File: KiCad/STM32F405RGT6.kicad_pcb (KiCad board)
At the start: 4 copper layers, 101.6 x 101.6 mm, 65 parts, among them J1 Conn_02x05_Odd_Even, J2 USB_C_2.0, J3 Conn_02x32_Odd_Even, J4 Conn_02x20_Odd_Even, Q1 AO3401A, SW1 TS-1187A, SW2 TS-1187A, U1 M24C02-RMN, U2 AMS1117-3.3, U3 STM32F405RGTx, Y1 16MHz

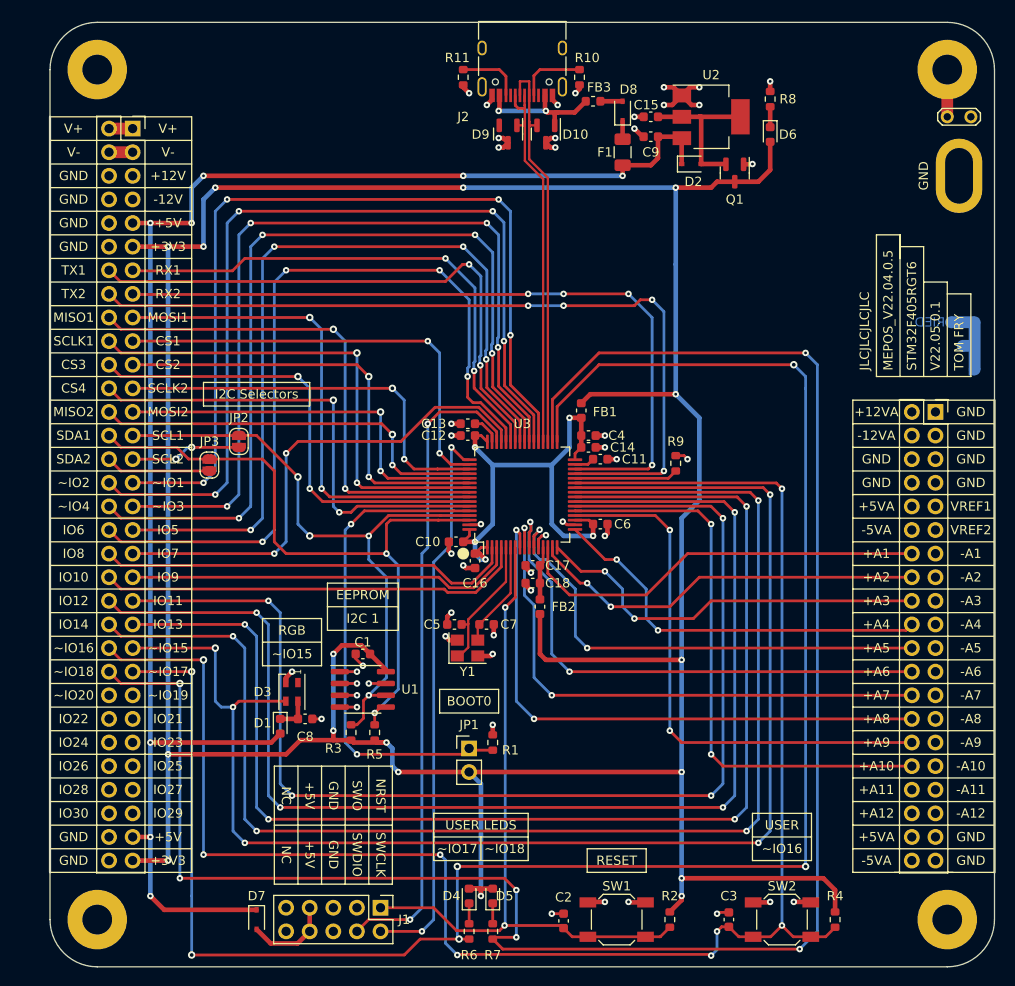
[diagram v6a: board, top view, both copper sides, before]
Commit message: Updated silkscreen text to labels
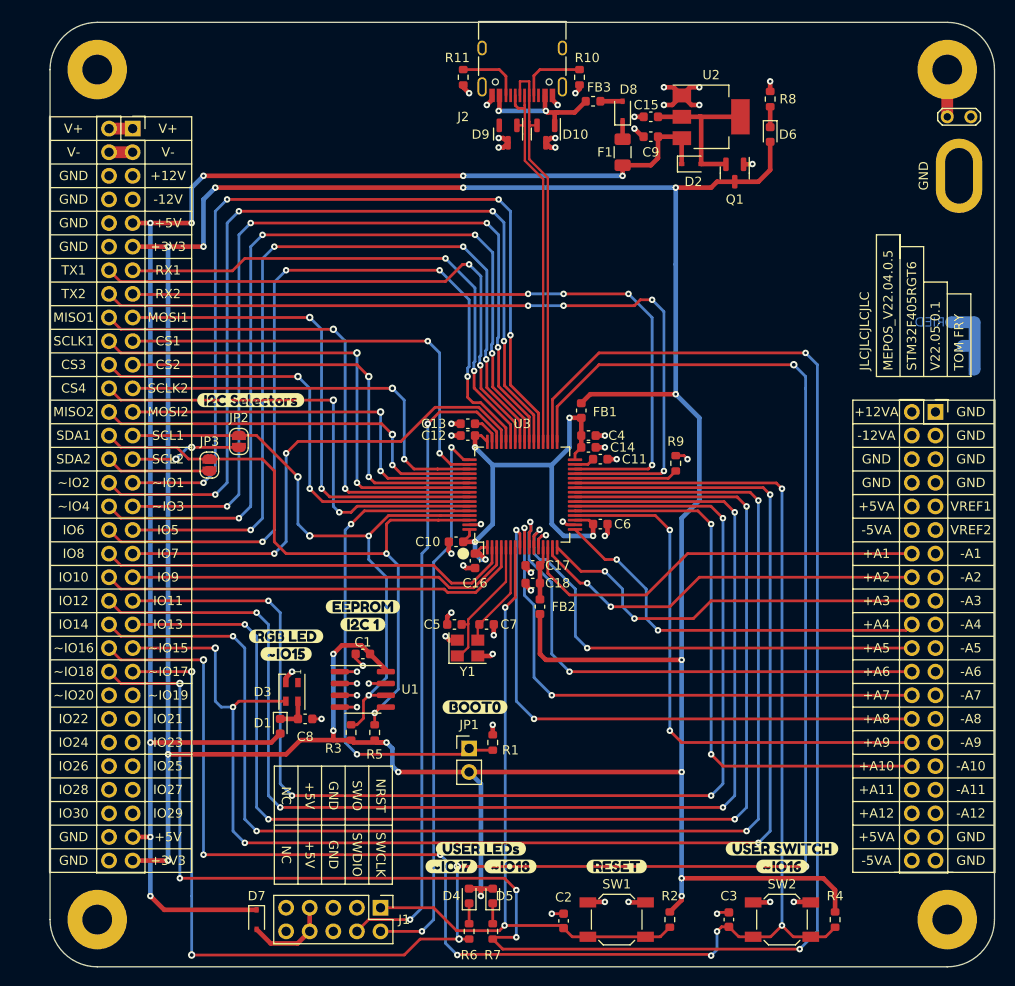
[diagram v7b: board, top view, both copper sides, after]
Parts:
- added kibuzzard-630B16ED: G***, kibuzzard-630B16ED, F.Cu at (59.2, 74.9)
- added kibuzzard-630B1710: G***, kibuzzard-630B1710, F.Cu at (71.3, 97.1)
- added kibuzzard-630B1728: G***, kibuzzard-630B1728, F.Cu at (71.3, 99.0)
- added kibuzzard-630B1736: G***, kibuzzard-630B1736, F.Cu at (63.0, 100.3)
- added kibuzzard-630B1749: G***, kibuzzard-630B1749, F.Cu at (63.0, 102.2)
- added kibuzzard-630B175D: G***, kibuzzard-630B175D, F.Cu at (83.3, 107.9)
- added kibuzzard-630B176C: G***, kibuzzard-630B176C, F.Cu at (98.6, 125.0)
- added kibuzzard-630B178A: G***, kibuzzard-630B178A, F.Cu at (116.3, 125.0)
- added kibuzzard-630B17C2: G***, kibuzzard-630B17C2, F.Cu at (116.3, 123.1)
- added kibuzzard-630B17D9: G***, kibuzzard-630B17D9, F.Cu at (87.1, 125.0)
- added kibuzzard-630B17E2: G***, kibuzzard-630B17E2, F.Cu at (80.8, 125.0)
- added kibuzzard-630B1806: G***, kibuzzard-630B1806, F.Cu at (84.0, 123.1)
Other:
- board text removed: "BOOT0"
- board text removed: "EEPROM"
- board text removed: "I2C 1"
- board text removed: "I2C Selectors"
- board text removed: "RESET"
- board text removed: "RGB"
- board text removed: "USER"
- board text removed: "USER LEDS"
